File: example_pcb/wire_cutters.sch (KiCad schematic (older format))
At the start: 7 parts, among them J1 Conn_01x02, J2 Conn_01x03, J3 Conn_01x03, Q1 2SCR293P, Q2 IRF-100S201

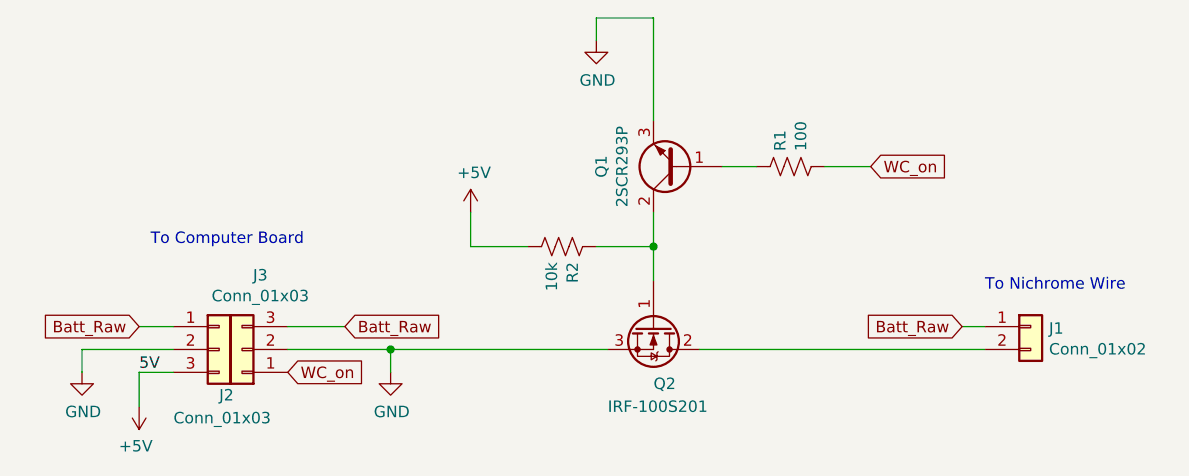
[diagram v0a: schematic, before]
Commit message: Removed the N-Channel Resistor from the schematic, netlist, and layout to be added as an example in lecture.
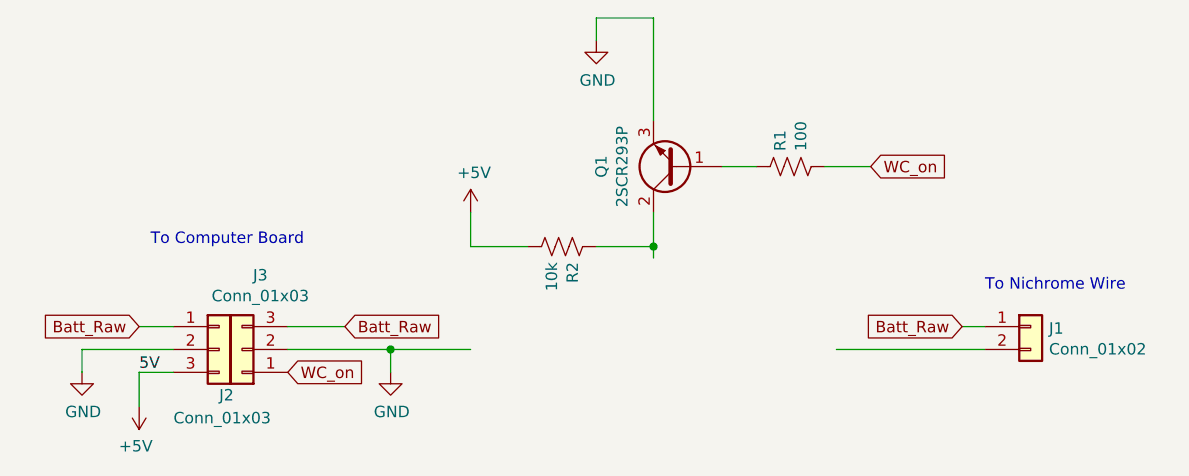
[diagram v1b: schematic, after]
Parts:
- removed Q2: IRF-100S201, Package_TO_SOT_SMD:TO-263-2, symbol Device:Q_NMOS_GDS
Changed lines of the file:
@@
 $EndDescr
-$Comp
-L Device:Q_NMOS_GDS Q2
-U 1 1 5DE81C62
-P 5850 4300
-F 0 "Q2" V 6100 4300 50  0000 L CNN
-F 1 "IRF-100S201" V 6200 4100 50  0000 L CNN
-F 2 "Package_TO_SOT_SMD:TO-263-2" H 6050 4400 50  0001 C CNN
-F 3 "~" H 5850 4300 50  0001 C CNN
-	1    5850 4300
-	0    1    1    0
-$EndComp
 $Comp
 L Transistor_BJT:2SD1047 Q1
@@
 	7200 4300 7300 4300
 Wire Wire Line
-	4700 4400 5650 4400
-Connection ~ 4700 4400
-Wire Wire Line
-	6050 4400 7300 4400
-Wire Wire Line
 	5850 3800 5850 3950
 Wire Wire Line
@@
 Wire Wire Line
 	5600 3950 5850 3950
-Connection ~ 5850 3950
-Wire Wire Line
-	5850 3950 5850 4100
 $Comp
 L power:+5V #PWR02
@@
 Text Notes 7300 4150 0    50   ~ 0
 To Nichrome Wire
+Wire Wire Line
+	4700 4400 5050 4400
+Connection ~ 4700 4400
+Wire Wire Line
+	7300 4400 6650 4400
+Wire Wire Line
+	5850 3950 5850 4000
+Connection ~ 5850 3950
 $EndSCHEMATC
